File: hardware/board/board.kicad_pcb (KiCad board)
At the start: 2 copper layers, 20 x 108 mm, 67 parts, among them J1 Power, J10 OUT B3, J12 IN C, J13 OUT C1, J14 OUT C2, J15 OUT C3, J17 OUT D, J18 IN D1, J19 IN D2, J2 IN A, J20 IN D3, J3 OUT A1, J4 OUT A2, J5 OUT A3, J7 IN B, J8 OUT B1, J9 OUT B2, U1 OPA4991, U2 OPA4991, U4 OPA4991, U6 OPA4991

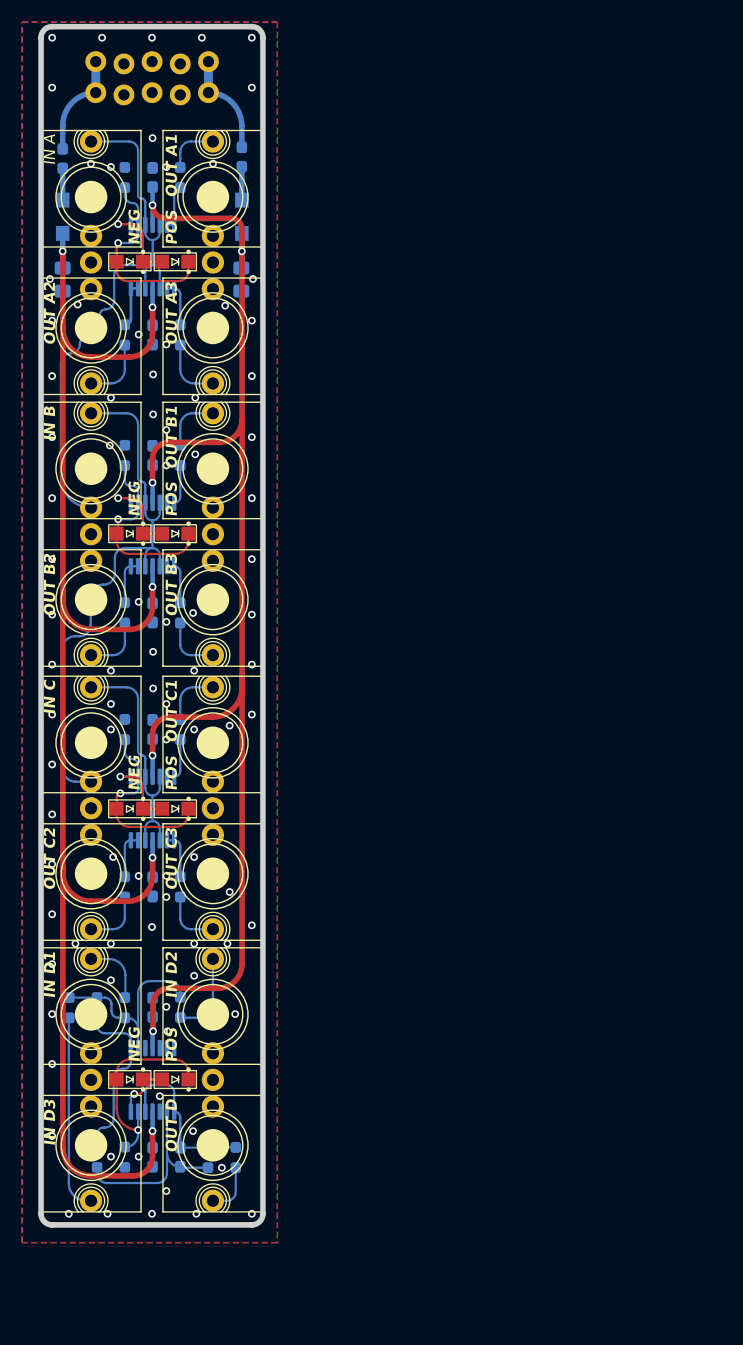
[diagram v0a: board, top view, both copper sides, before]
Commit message: hardware: Changes for self-sourcing
- Add manufacturer part numbers and DigiKey, Mouser, and LCSC part numbers for all BOM items.
- Split schematic into multiple US letter-sized sheets.
- Update to new Winterbloom drawing sheet.
- Create new PDF of schematic.
- Create gerbers.zip with pre-made Gerbers.
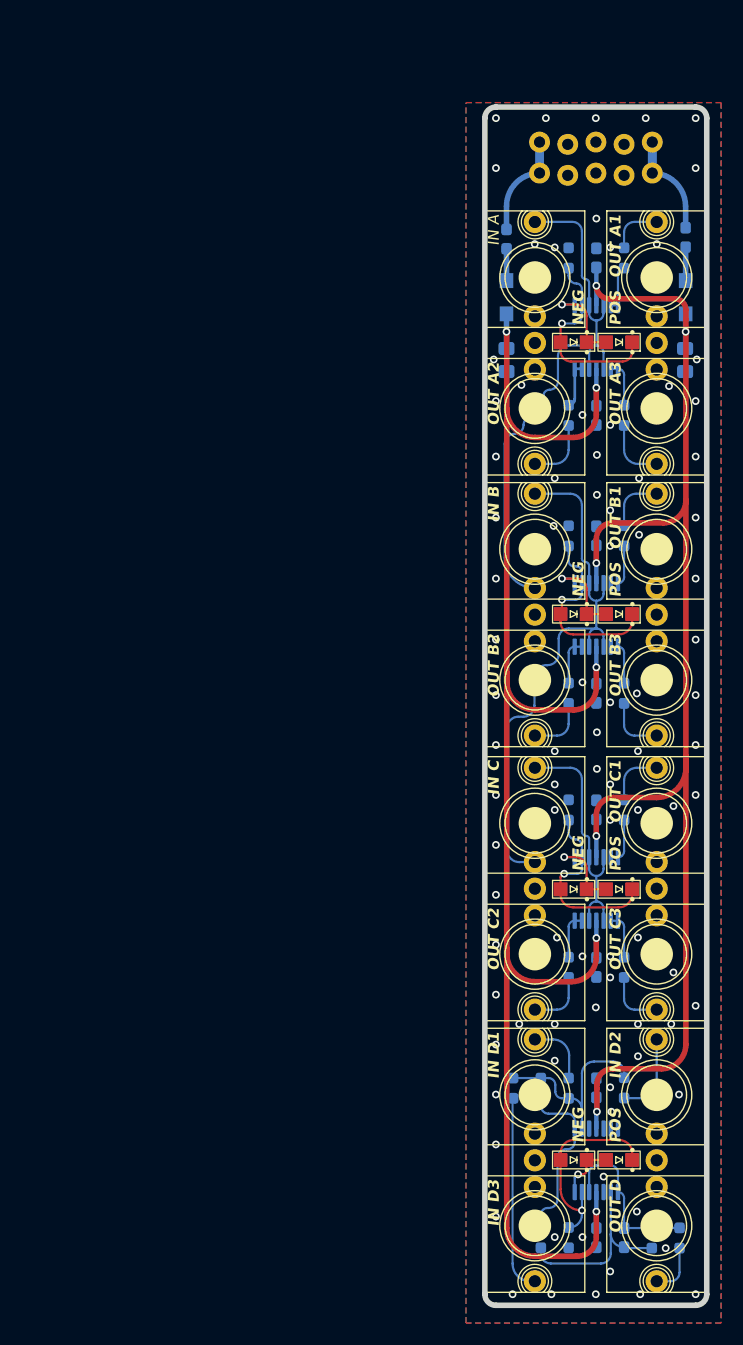
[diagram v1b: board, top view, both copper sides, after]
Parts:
- R10, R11, R16, R9: value 1.5k -> 1k5
- moved J1 40.7 mm to (133.8, 58.5)
- moved R9 40.7 mm to (136.4, 68.8)
- moved ? 40.7 mm to (132.4, 119.2)
- moved C2 40.7 mm to (130.8, 78.0)
- moved D1 40.7 mm to (130.8, 72.3)
- moved D10 40.7 mm to (136.9, 150.1)
- moved D2 40.7 mm to (147.0, 72.3)
- moved D3 40.7 mm to (141.0, 76.4)
- moved D4 40.7 mm to (136.9, 76.4)
- moved D5 40.7 mm to (141.0, 100.9)
- moved D6 40.7 mm to (136.9, 100.9)
- moved D7 40.7 mm to (141.0, 125.7)
- moved D8 40.7 mm to (136.9, 125.7)
- moved D9 40.7 mm to (141.0, 150.1)
- moved J12 40.7 mm to (133.4, 119.8)
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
